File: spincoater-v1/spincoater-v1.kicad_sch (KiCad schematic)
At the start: 36 parts, among them J1 Conn_01x08_Pin, J2 Conn_01x03_Socket, J3 Conn_01x06_Socket, J4 Conn_01x03_Socket, J5 Conn_01x04_Pin, J6 LED_Conn_01x02_Pin, J7 LED_Conn_01x02_Pin, J8 12V_DC_Conn_01x02_Pin, Q1 IRF9540N, Q2 2N2222A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

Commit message: made some final changes to schematic and the fingerprints, might still need to change a few polarized caps
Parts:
- removed U2: LCD-16X2, LCD-16X2:MODULE_LCD-16X2, symbol LCD-16X2:LCD-16X2
- added J9: LCD_Conn_01x16_Socket, Connector_PinSocket_2.54mm:PinSocket_1x16_P2.54mm_Vertical, symbol Connector:Conn_01x16_Socket
- C1, C2, C4, C5, C6: footprint (none) -> Capacitor_SMD:C_0603_1608Metric_Pad1.08x0.95mm_HandSolder
- C3, C7: footprint (none) -> Capacitor_THT:CP_Radial_D13.0mm_P5.00mm
- F1: footprint (none) -> Fuse:Fuseholder_Keystone_3555-2
- J1: value Conn_01x08_Pin -> KEYPAD_Conn_01x08_Pin; footprint (none) -> Connector_PinSocket_2.54mm:PinSocket_1x08_P2.54mm_Vertical
- J2: value Conn_01x03_Socket -> POT_PIN28_Conn_01x03_Socket; footprint (none) -> Connector_PinSocket_2.54mm:PinSocket_1x03_P2.54mm_Vertical
- J3: value Conn_01x06_Socket -> SDCARD_Conn_01x06_Socket; footprint (none) -> Connector_PinSocket_2.54mm:PinSocket_1x06_P2.54mm_Vertical
- J4: value Conn_01x03_Socket -> POT_PIN27_Conn_01x03_Socket; footprint (none) -> Connector_PinSocket_2.54mm:PinSocket_1x03_P2.54mm_Vertical
- J5: value Conn_01x04_Pin -> MOTOR_Conn_01x04_Pin; footprint (none) -> Connector_PinHeader_2.54mm:PinHeader_1x04_P2.54mm_Vertical
- J6: value LED_Conn_01x02_Pin -> LED1_Conn_01x02_Pin; footprint (none) -> Connector_PinHeader_2.54mm:PinHeader_1x02_P2.54mm_Vertical
- J7: value LED_Conn_01x02_Pin -> LED2_Conn_01x02_Pin; footprint (none) -> Connector_PinHeader_2.54mm:PinHeader_1x02_P2.54mm_Vertical
- J8: footprint (none) -> Connector_PinHeader_2.54mm:PinHeader_1x02_P2.54mm_Vertical
- R1, R2, R3, R4, R5, R6: footprint (none) -> Resistor_SMD:R_0603_1608Metric_Pad0.98x0.95mm_HandSolder
- RV1, RV2: footprint (none) -> Potentiometer_THT:Potentiometer_Runtron_RM-065_Vertical
- U1: footprint RASPBERRY_PI_PICO:RASPBERRY_PI_PICO -> rpi_pico:RPI_PICO
- U3: footprint (none) -> Package_TO_SOT_THT:TO-220-3_Vertical
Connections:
- net GND: now also J9.1 (Pin_1), J9.16 (Pin_16), J9.5 (Pin_5)
- net LCD.A: now also J9.15 (Pin_15)
- net LCD.D4: now also J9.11 (Pin_11)
- net LCD.D5: now also J9.12 (Pin_12)
- net LCD.D6: now also J9.13 (Pin_13)
- net LCD.D7: now also J9.14 (Pin_14)
- net LCD.E: now also J9.6 (Pin_6)
- net LCD.RS: now also J9.4 (Pin_4)
- net LCD.VDD: now also J9.2 (Pin_2)
- net LCD.VO: now also J9.3 (Pin_3)
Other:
- moved on the sheet: J3

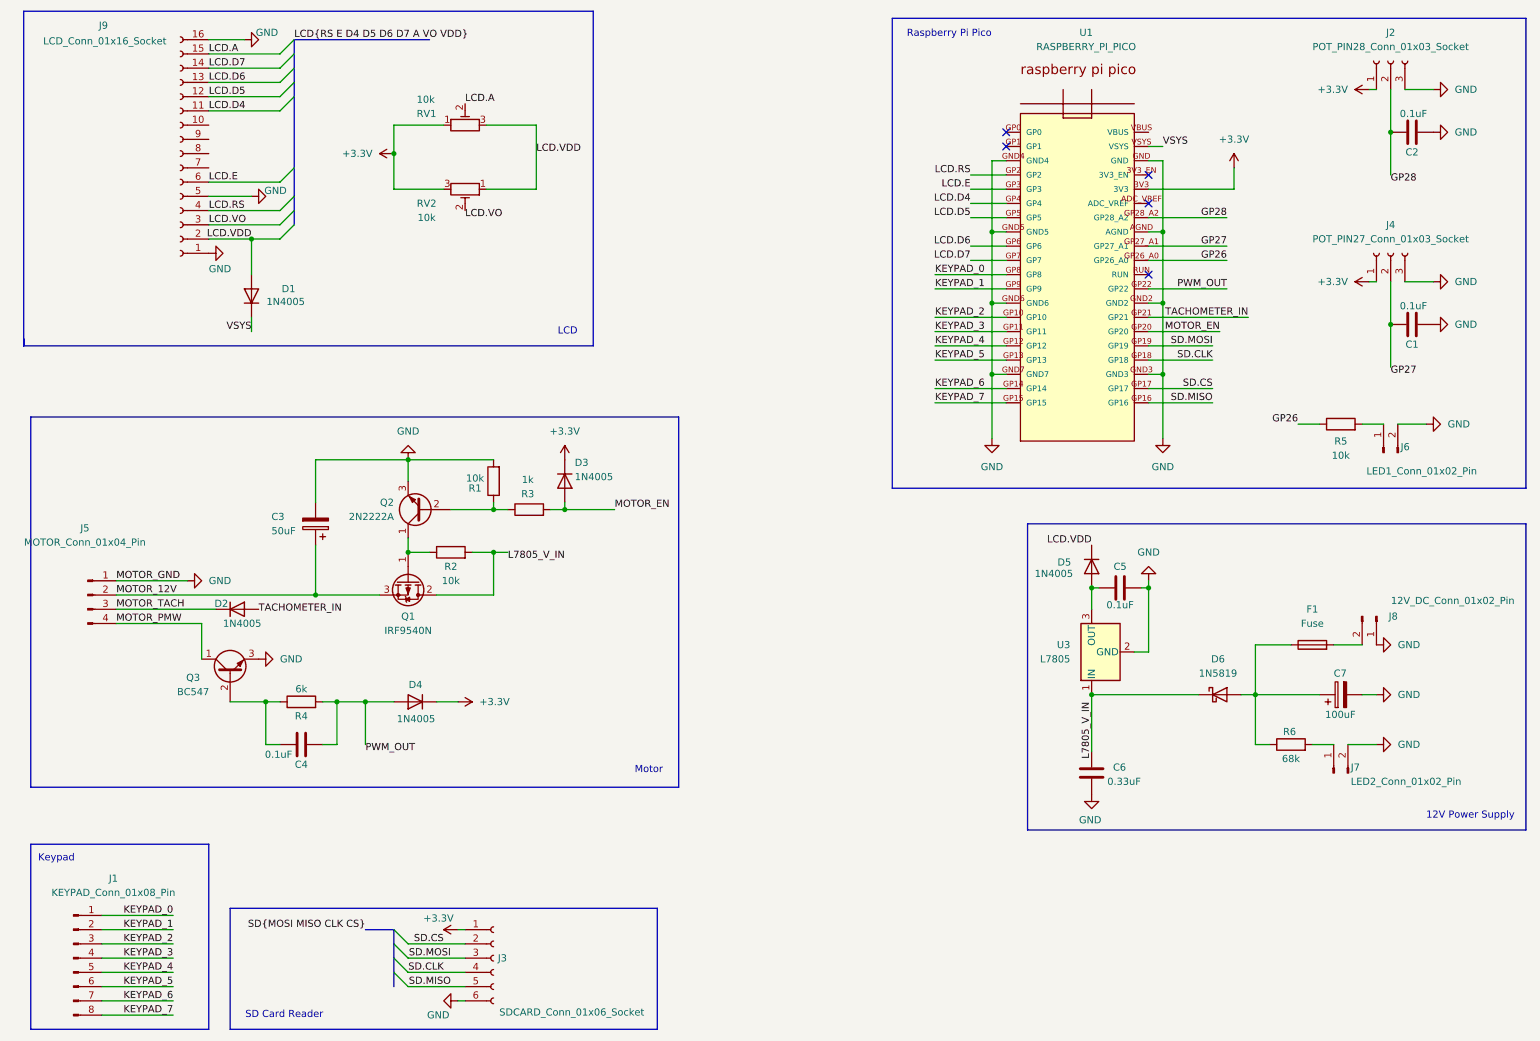
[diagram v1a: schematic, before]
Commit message: Organized the pcb layout a bit, not sure if it is ideal. Ran the PCB through auto routing. Changed transistors to horizontal orrientation so that we can attach the LCD screen directly to the PCB. The capacitors might need to be changed, still don't know what size to use for it. Also might need to turn the capacitors horizontal for space saving purposes.
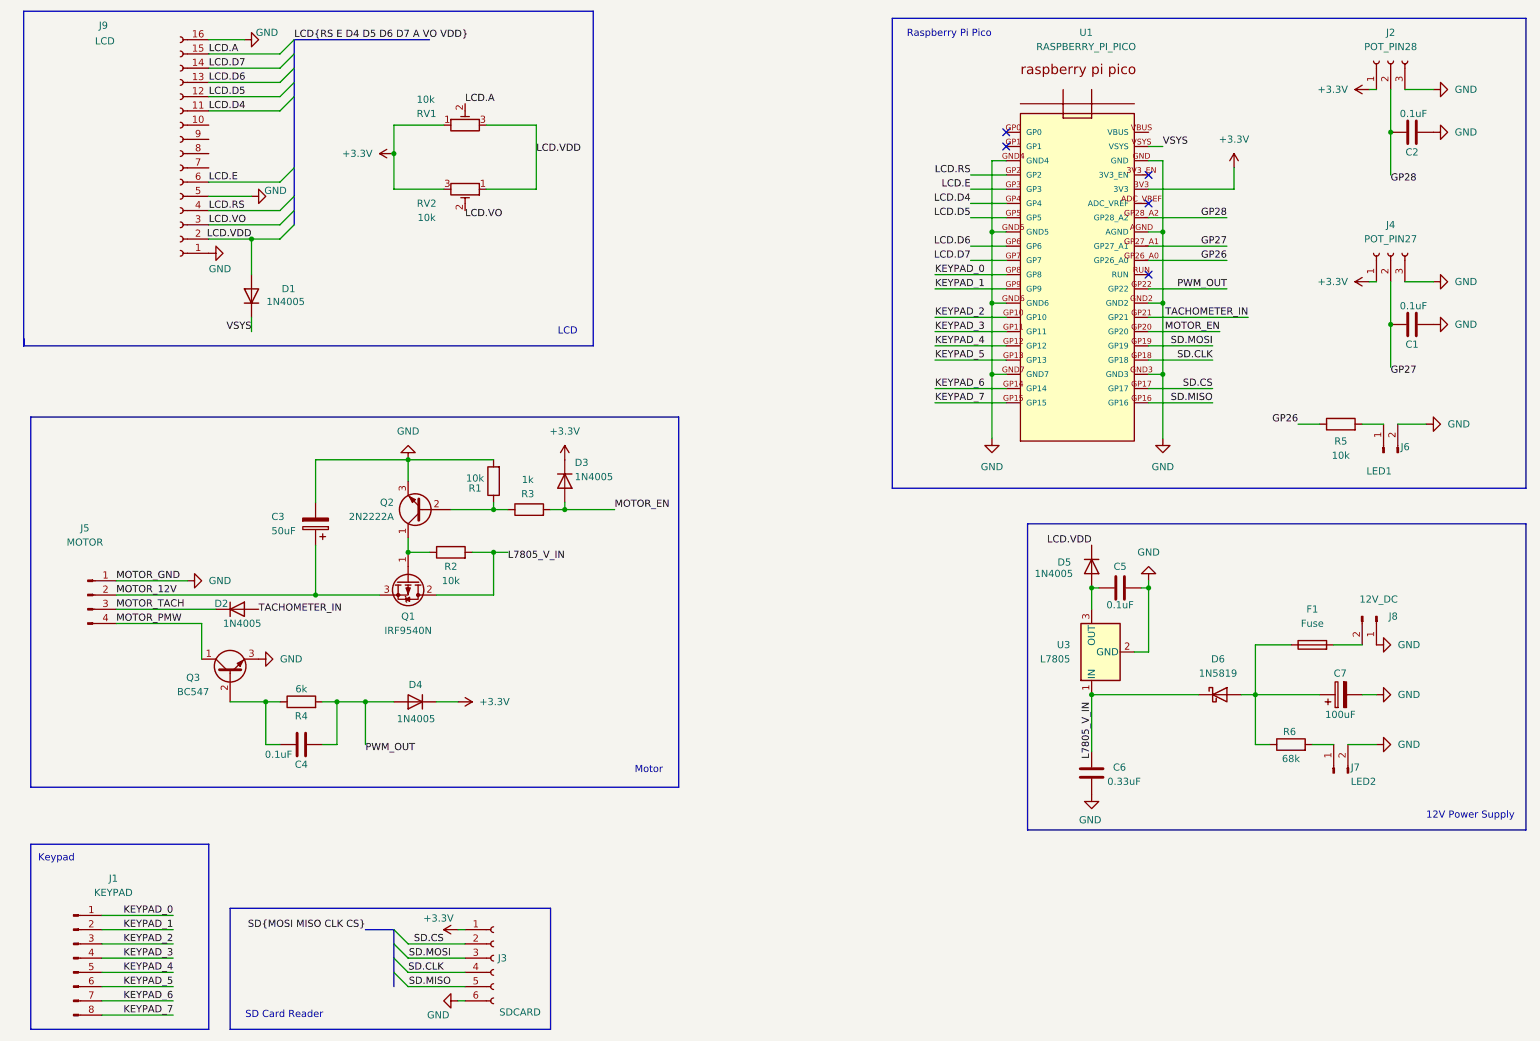
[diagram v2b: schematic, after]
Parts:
- J1: value KEYPAD_Conn_01x08_Pin -> KEYPAD
- J2: value POT_PIN28_Conn_01x03_Socket -> POT_PIN28
- J3: value SDCARD_Conn_01x06_Socket -> SDCARD
- J4: value POT_PIN27_Conn_01x03_Socket -> POT_PIN27
- J5: value MOTOR_Conn_01x04_Pin -> MOTOR
- J6: value LED1_Conn_01x02_Pin -> LED1
- J7: value LED2_Conn_01x02_Pin -> LED2
- J8: value 12V_DC_Conn_01x02_Pin -> 12V_DC
- J9: value LCD_Conn_01x16_Socket -> LCD
- Q1, U3: footprint Package_TO_SOT_THT:TO-220-3_Vertical -> Package_TO_SOT_THT:TO-220-3_Horizontal_TabUp
- Q2, Q3: footprint Package_TO_SOT_THT:TO-92_Inline -> Package_TO_SOT_THT:TO-92_Inline_Horizontal1

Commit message: fixed trace issue
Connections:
- net +3.3V: no longer RV1.1, RV2.3
- net GND: now also RV1.1, RV2.3
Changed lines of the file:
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@@
 	)
 	(junction
-		(at 80.01 39.37)
-		(diameter 0)
-		(color 0 0 0 0)
-	)
-	(junction
 		(at 186.69 78.74)
 		(diameter 0)
@@
 	)
 	(junction
+		(at 80.01 39.37)
+		(diameter 0)
+		(color 0 0 0 0)
+	)
+	(junction
 		(at 69.85 137.16)
 		(diameter 0)
@@
 		)
 	)
-	(wire
+	(bus
 		(pts
-			(xy 80.01 34.29) (xy 80.01 39.37)
+			(xy 62.23 19.05) (xy 62.23 21.59)
 		)
 		(stroke
@@
 		)
 	)
-	(bus
+	(wire
 		(pts
-			(xy 62.23 19.05) (xy 62.23 21.59)
+			(xy 80.01 34.29) (xy 80.01 39.37)
 		)
 		(stroke
@@
 		)
 	)
+	(wire
+		(pts
+			(xy 80.01 39.37) (xy 80.01 45.72)
+		)
+		(stroke
+			(width 0)
+			(type default)
+		)
+	)
 	(bus
 		(pts
@@
 	(wire
 		(pts
-			(xy 80.01 39.37) (xy 80.01 45.72)
-		)
-		(stroke
-			(width 0)
-			(type default)
-		)
-	)
-	(wire
-		(pts
 			(xy 82.55 180.34) (xy 92.71 180.34)
 		)
@@
 	)
 	(symbol
-		(lib_id "power:+3.3V")
-		(at 80.01 39.37 90)
-		(unit 1)
-		(exclude_from_sim no)
-		(in_bom yes)
-		(on_board yes)
-		(dnp no)
-		(fields_autoplaced yes)
-		(property "Reference" "#PWR03"
-			(at 83.82 39.37 0)
-			(effects
-				(font
-					(size 1.27 1.27)
-				)
-				(hide yes)
-			)
-		)
-		(property "Value" "+3.3V"
-			(at 76.2 39.3699 90)
-			(effects
-				(font
-					(size 1.27 1.27)
-				)
-				(justify left)
-			)
-		)
-		(property "Footprint" ""
-			(at 80.01 39.37 0)
-			(effects
-				(font
-					(size 1.27 1.27)
-				)
-				(hide yes)
-			)
-		)
-		(property "Datasheet" ""
-			(at 80.01 39.37 0)
-			(effects
-				(font
-					(size 1.27 1.27)
-				)
-				(hide yes)
-			)
-		)
-		(property "Description" "Power symbol creates a global label with name \"+3.3V\""
-			(at 80.01 39.37 0)
-			(effects
-				(font
-					(size 1.27 1.27)
-				)
-				(hide yes)
-			)
-		)
-		(pin "1"
-		)
-		(instances
-			(project ""
-				(path "/0002d598-dc76-4eaf-98b0-aaba33fc6972"
-					(reference "#PWR03")
-					(unit 1)
-				)
-			)
-		)
-	)
-	(symbol
 		(lib_id "power:GND")
 		(at 264.16 87.63 90)
@@
 					(unit 1)
 				)
+			)
+		)
+	)
+	(symbol
+		(lib_id "power:GND")
+		(at 80.01 39.37 270)
+		(unit 1)
+		(exclude_from_sim no)
+		(in_bom yes)
+		(on_board yes)
+		(dnp no)
+		(fields_autoplaced yes)
+		(property "Reference" "#PWR03"
+			(at 73.66 39.37 0)
+			(effects
+				(font
+					(size 1.27 1.27)
+				)
+				(hide yes)
+			)
+		)
+		(property "Value" "GND"
+			(at 76.2 39.3699 90)
+			(effects
+				(font
+					(size 1.27 1.27)
+				)
+				(justify right)
+			)
+		)
+		(property "Footprint" ""
+			(at 80.01 39.37 0)
+			(effects
+				(font
+					(size 1.27 1.27)
+				)
+				(hide yes)
+			)
+		)
+		(property "Datasheet" ""
+			(at 80.01 39.37 0)
+			(effects
+				(font
+					(size 1.27 1.27)
+				)
+				(hide yes)
+			)
+		)
+		(property "Description" "Power symbol creates a global label with name \"GND\" , ground"
+			(at 80.01 39.37 0)
+			(effects
+				(font
+					(size 1.27 1.27)
+				)
+				(hide yes)
+			)
+		)
+		(pin "1"
+		)
+		(instances
+			(project ""
+				(path "/0002d598-dc76-4eaf-98b0-aaba33fc6972"
+					(reference "#PWR03")
+					(unit 1)
+				)
